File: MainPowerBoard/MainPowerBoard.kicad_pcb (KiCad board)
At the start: 2 copper layers, 177.8 x 177.8 mm, 259 parts, among them J101 CONN_01X04, J102 CONN_01X04, J103 CONN_01X04, J104 CONN_01X02, J105 CONN_01X02, J106 CONN_01X06, J107 CONN_01X06, J108 CONN_01X04, J109 CONN_01X04, J110 CONN_01X02, J111 CONN_01X02, J112 CONN_01X02, J113 CONN_01X02, J114 CONN_01X02, J115 CONN_01X02, J116 CONN_01X02, J117 CONN_01X02, J118 CONN_01X02, J119 CONN_01X02, J120 CONN_01X02, J121 CONN_01X02, J122 CONN_01X02, J123 CONN_01X02, J124 CONN_01X02, J125 CONN_01X02, J126 CONN_01X02, J127 CONN_01X02, J128 CONN_01X02, J129 CONN_01X02, J130 MOUNTING_HOLE, J131 MOUNTING_HOLE, J132 MOUNTING_HOLE, J133 MOUNTING_HOLE, Q1 CSD19502Q5B, Q2 CSD19502Q5B, SW701 KS-01Q-01, U1 LTC4357MPMS8, U1001 LMR16030S, U1101 LMR16030S, U1201 LMR16030S, U1301 LMR16030S, U1401 LMR16030S, U2 LTC4357MPMS8, U201 LMR16030S, U301 LMR16030S, U701 AP2204RA-5.0TRG1, U702 TLV271IDBVR, U703 LTC2950-1, U704 TLC393, U801 LMR16030S, U901 LMR16030S

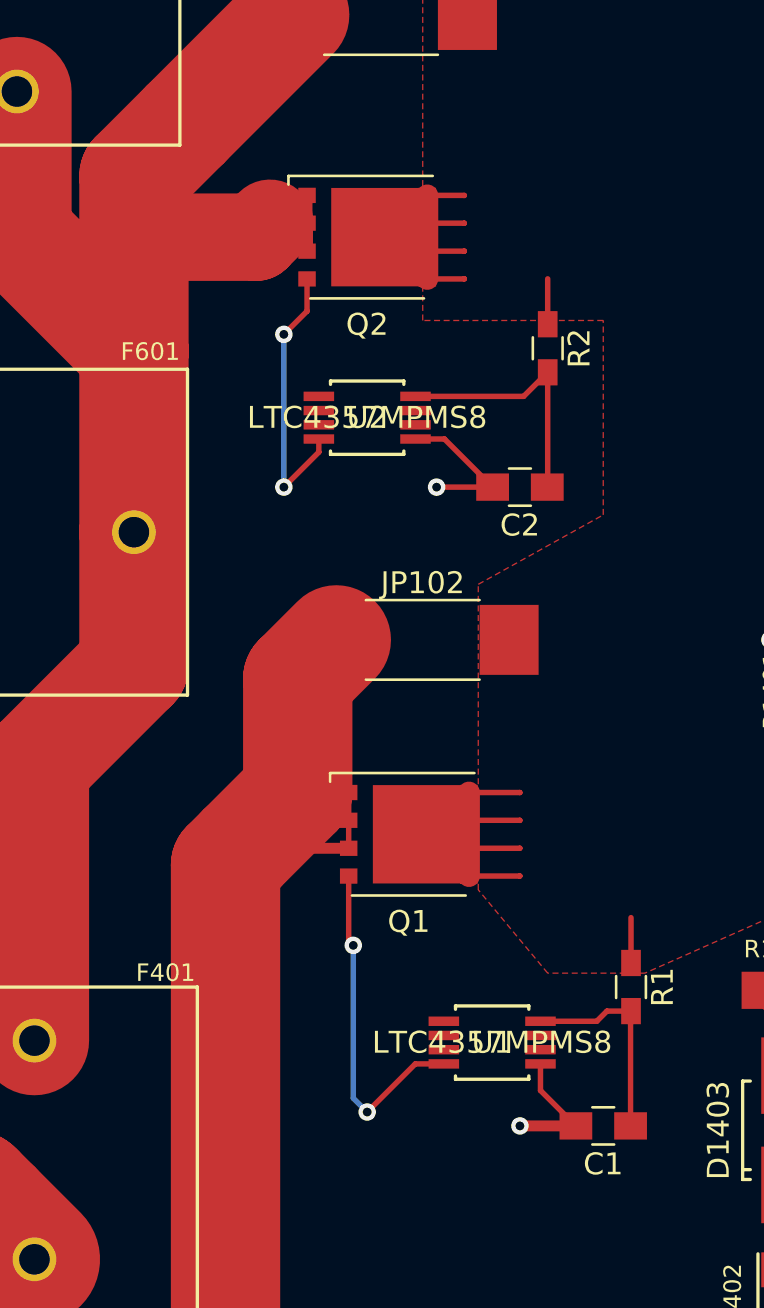
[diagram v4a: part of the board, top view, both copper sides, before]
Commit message: Fixed grounding of bat output and connected missing ground connection on LTC chip
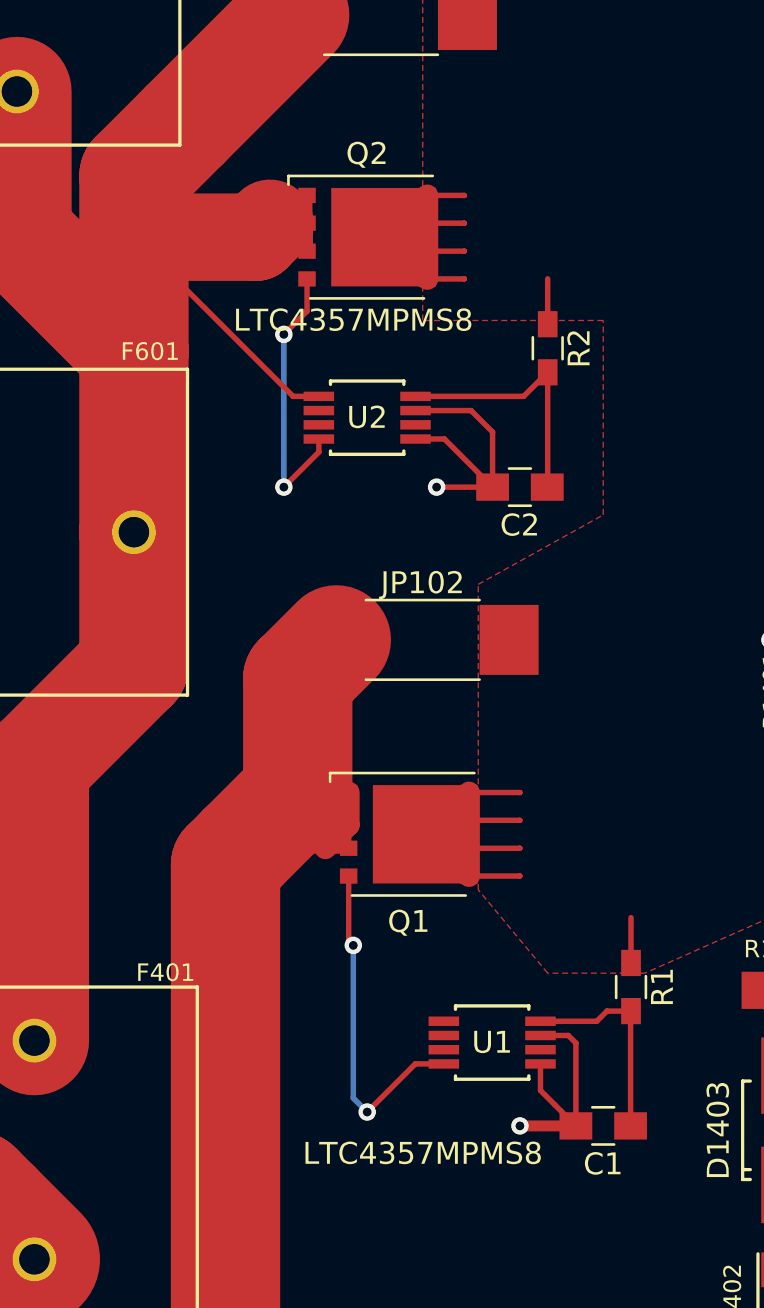
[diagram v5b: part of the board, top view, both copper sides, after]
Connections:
- F401 pad 2: GND -> /VCC_BATT_COMB
- F501 pad 2: GND -> /VCC_BATT_COMB
- F601 pad 2: GND -> /VCC_BATT_COMB
- JP103 pad 1: GND -> /VCC_BATT_COMB
- Q2 pad 1: GND -> /VCC_BATT_COMB
- Q2 pad 2: GND -> /VCC_BATT_COMB
- Q2 pad 3: GND -> /VCC_BATT_COMB
- U2 pad 1: GND -> /VCC_BATT_COMB
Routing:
- net /VCC_BATT_COMB: track 0.00 -> 87.7 mm
- net GND: track 698.8 -> 634.6 mm
- net /48V0_FROM_LINE: track 44.9 -> 47.9 mm
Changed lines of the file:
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@@
 (kicad_pcb (version 4) (host pcbnew 4.0.6)
   (general
-    (links 982)
-    (no_connects 356)
+    (links 981)
+    (no_connects 353)
     (area -6.075 -6.075 183.285 183.285)
     (thickness 1.6)
     (drawings 83)
-    (tracks 2097)
+    (tracks 2109)
     (zones 0)
     (modules 259)
-    (nets 151)
+    (nets 152)
   )
   (page B)
@@
   )
   (setup
-    (last_trace_width 0.5)
+    (last_trace_width 1)
     (user_trace_width 0.5)
     (user_trace_width 1)
@@
   (net 149 "/5 Volt Regulator -- 2/24V0_REG")
   (net 150 "Net-(D1402-Pad1)")
+  (net 151 /VCC_BATT_COMB)
   (net_class Default "This is the default net class."
     (clearance 0.2)
@@
     (add_net /STATE)
     (add_net /SW_HI)
+    (add_net /VCC_BATT_COMB)
     (add_net GND)
     (add_net "Net-(C1-Pad1)")
@@
       (net 77 "Net-(D401-Pad2)"))
     (pad 2 thru_hole circle (at 12.45 -7.45 90) (size 2 2) (drill 1.4) (layers *.Cu *.Mask)
-      (net 1 GND))
+      (net 151 /VCC_BATT_COMB))
   )
   (module CONN_PHOENIX_1844252_6PIN (layer F.Cu)
@@
       (net 81 "Net-(D601-Pad2)"))
     (pad 2 thru_hole circle (at 12.45 -7.45) (size 2 2) (drill 1.4) (layers *.Cu *.Mask)
-      (net 1 GND))
+      (net 151 /VCC_BATT_COMB))
   )
   (module Diodes_SMD:SMB_Handsoldering (layer F.Cu)
@@
       (net 79 "Net-(D501-Pad2)"))
     (pad 2 thru_hole circle (at 12.45 -7.45 270) (size 2 2) (drill 1.4) (layers *.Cu *.Mask)
-      (net 1 GND))
+      (net 151 /VCC_BATT_COMB))
   )
   (module hyperCustom:TP_SMT_Keystone (layer F.Cu)
@@
     (fp_line (start 5.55 1.85) (end -5.56 1.85) (layer F.CrtYd) (width 0.05))
     (pad 1 smd rect (at -3.95 0) (size 2.7 3.2) (layers F.Cu F.Paste F.Mask)
-      (net 1 GND))
+      (net 151 /VCC_BATT_COMB))
     (pad 2 smd rect (at 3.95 0) (size 2.7 3.2) (layers F.Cu F.Paste F.Mask)
       (net 126 /MAIN_POWER))
@@
     (tags "tdson ")
     (attr smd)
-    (fp_text reference Q2 (at 0 4) (layer F.SilkS)
+    (fp_text reference Q2 (at 0 -3.81) (layer F.SilkS)
       (effects (font (size 1 1) (thickness 0.15)))
     )
@@
     (fp_line (start -2 -2.6) (end -3 -1.6) (layer F.Fab) (width 0.1))
     (pad 1 smd rect (at -2.75 -1.91 270) (size 0.7 0.8) (layers F.Cu F.Paste F.Mask)
-      (net 1 GND))
+      (net 151 /VCC_BATT_COMB))
     (pad 2 smd rect (at -2.75 -0.64 270) (size 0.7 0.8) (layers F.Cu F.Paste F.Mask)
-      (net 1 GND))
+      (net 151 /VCC_BATT_COMB))
     (pad 3 smd rect (at -2.75 0.64 270) (size 0.7 0.8) (layers F.Cu F.Paste F.Mask)
-      (net 1 GND))
+      (net 151 /VCC_BATT_COMB))
     (pad 4 smd rect (at -2.75 1.91 270) (size 0.7 0.8) (layers F.Cu F.Paste F.Mask)
       (net 130 "Net-(Q2-Pad4)"))
@@
       (effects (font (size 1 1) (thickness 0.15)))
     )
-    (fp_text value LTC4357MPMS8 (at 0 0) (layer F.SilkS)
+    (fp_text value LTC4357MPMS8 (at -3.175 5.08) (layer F.SilkS)
       (effects (font (size 1 1) (thickness 0.15)))
     )
@@
     (fp_arc (start 0 -1.5494) (end 0.3048 -1.5494) (angle 180) (layer Dwgs.User) (width 0.1524))
     (pad 1 smd rect (at -2.2098 -0.974999) (size 1.397 0.4318) (layers F.Cu)
-      (net 28 /48V0_FROM_LINE))
+      (net 28 /48V0_FROM_LINE) (clearance 0.1))
     (pad 2 smd rect (at -2.2098 -0.325001) (size 1.397 0.4318) (layers F.Cu)
-      (net 131 "Net-(U1-Pad2)"))
+      (net 131 "Net-(U1-Pad2)") (clearance 0.1))
     (pad 3 smd rect (at -2.2098 0.325001) (size 1.397 0.4318) (layers F.Cu)
-      (net 132 "Net-(U1-Pad3)"))
+      (net 132 "Net-(U1-Pad3)") (clearance 0.1))
     (pad 4 smd rect (at -2.2098 0.974999) (size 1.397 0.4318) (layers F.Cu)
-      (net 129 "Net-(Q1-Pad4)"))
+      (net 129 "Net-(Q1-Pad4)") (clearance 0.1))
     (pad 5 smd rect (at 2.2098 0.974999) (size 1.397 0.4318) (layers F.Cu)
       (net 1 GND))
@@
       (effects (font (size 1 1) (thickness 0.15)))
     )
-    (fp_text value LTC4357MPMS8 (at 0 0) (layer F.SilkS)
+    (fp_text value LTC4357MPMS8 (at -0.635 -4.445) (layer F.SilkS)
       (effects (font (size 1 1) (thickness 0.15)))
     )
@@
     (fp_arc (start 0 -1.5494) (end 0.3048 -1.5494) (angle 180) (layer Dwgs.User) (width 0.1524))
     (pad 1 smd rect (at -2.2098 -0.974999) (size 1.397 0.4318) (layers F.Cu)
-      (net 1 GND) (clearance 0.1))
+      (net 151 /VCC_BATT_COMB) (clearance 0.1))
     (pad 2 smd rect (at -2.2098 -0.325001) (size 1.397 0.4318) (layers F.Cu)
       (net 134 "Net-(U2-Pad2)") (clearance 0.1))
@@
   (gr_line (start 177.8 0) (end 177.8 177.8) (angle 90) (layer Edge.Cuts) (width 0.15))
   (gr_line (start 0 0) (end 177.8 0) (angle 90) (layer Edge.Cuts) (width 0.15))
-  (segment (start 53.765 87) (end 53.765 84.45) (width 0.5) (layer F.Cu) (net 1) (status C00000))
-  (segment (start 45.85 86.36) (end 51.435 86.36) (width 4) (layer F.Cu) (net 1))
-  (segment (start 51.435 86.36) (end 52.07 85.725) (width 4) (layer F.Cu) (net 1))
+  (segment (start 64.4398 122.864999) (end 65.714999 122.864999) (width 0.25) (layer F.Cu) (net 1))
+  (segment (start 66.06 123.21) (end 66.06 127) (width 0.25) (layer F.Cu) (net 1))
+  (segment (start 65.714999 122.864999) (end 66.06 123.21) (width 0.25) (layer F.Cu) (net 1))
+  (segment (start 58.7248 94.289999) (end 61.269999 94.289999) (width 0.25) (layer F.Cu) (net 1))
+  (segment (start 62.25 95.27) (end 62.25 97.79) (width 0.25) (layer F.Cu) (net 1))
+  (segment (start 61.269999 94.289999) (end 62.25 95.27) (width 0.25) (layer F.Cu) (net 1))
   (segment (start 62.25 97.79) (end 59.69 97.79) (width 0.25) (layer F.Cu) (net 1))
   (via (at 59.69 97.79) (size 0.8) (drill 0.4) (layers F.Cu B.Cu) (net 1))
@@
   (via (at 63.5 127) (size 0.8) (drill 0.4) (layers F.Cu B.Cu) (net 1))
   (segment (start 64.4398 124.164999) (end 64.4398 125.3798) (width 0.25) (layer F.Cu) (net 1))
-  (segment (start 64.4398 125.3798) (end 66.06 127) (width 0.25) (layer F.Cu) (net 1))
+  (segment (start 64.4398 125.3798) (end 65.0975 126.0375) (width 0.25) (layer F.Cu) (net 1))
+  (segment (start 65.0975 126.0375) (end 66.06 127) (width 0.25) (layer F.Cu) (net 1))
   (via (at 93.38 67.945) (size 1) (drill 0.3) (layers F.Cu B.Cu) (net 1))
   (via (at 95.38 65.245) (size 1) (drill 0.3) (layers F.Cu B.Cu) (net 1))
@@
   (via (at 88.235 117.2) (size 1) (drill 0.3) (layers F.Cu B.Cu) (net 1))
   (via (at 89.835 114.7) (size 1) (drill 0.3) (layers F.Cu B.Cu) (net 1))
-  (segment (start 53.765 87) (end 53.765 85.72) (width 0.5) (layer F.Cu) (net 1))
-  (segment (start 45.85 91.57) (end 45.85 86.36) (width 5) (layer F.Cu) (net 1))
-  (segment (start 48.19 81.21) (end 53.2 76.2) (width 5) (layer F.Cu) (net 1))
-  (segment (start 45.85 83.55) (end 48.19 81.21) (width 5) (layer F.Cu) (net 1))
-  (segment (start 45.85 86.36) (end 45.85 83.55) (width 5) (layer F.Cu) (net 1))
-  (segment (start 40.5 79.7) (end 40.5 86.22) (width 5) (layer F.Cu) (net 1))
-  (segment (start 45.85 91.57) (end 45.85 99.85) (width 5) (layer F.Cu) (net 1))
-  (segment (start 40.5 86.22) (end 45.85 91.57) (width 5) (layer F.Cu) (net 1))
-  (segment (start 41.3 123.1) (end 41.3 110.515) (width 5) (layer F.Cu) (net 1))
-  (segment (start 45.85 105.965) (end 45.85 99.85) (width 5) (layer F.Cu) (net 1))
-  (segment (start 41.3 110.515) (end 45.85 105.965) (width 5) (layer F.Cu) (net 1))
   (via (at 83.335 125.4) (size 0.8) (drill 0.4) (layers F.Cu B.Cu) (net 1))
   (segment (start 82.985 125.75) (end 83.335 125.4) (width 0.25) (layer F.Cu) (net 1))
@@
   (segment (start 130.48014 168.2) (end 126.59936 168.2) (width 0.25) (layer F.Cu) (net 26))
   (segment (start 75.435 139.6) (end 75.435 136.41986) (width 0.25) (layer F.Cu) (net 27))
-  (segment (start 55.67 114.305) (end 50.795 114.305) (width 0.5) (layer F.Cu) (net 28))
+  (segment (start 55.67 111.755) (end 55.67 113.24) (width 1) (layer F.Cu) (net 28) (status C00000))
+  (segment (start 55.67 113.24) (end 54.605 114.305) (width 1) (layer F.Cu) (net 28) (status 400000))
+  (segment (start 55.67 114.305) (end 54.605 114.305) (width 0.5) (layer F.Cu) (net 28))
+  (segment (start 54.605 114.305) (end 50.795 114.305) (width 0.5) (layer F.Cu) (net 28))
   (segment (start 50.795 114.305) (end 50.8 114.3) (width 0.5) (layer F.Cu) (net 28))
   (segment (start 55.67 111.755) (end 55.67 113.025) (width 0.25) (layer F.Cu) (net 28))
@@
   (segment (start 79.685 136.55) (end 84.035 140.9) (width 3) (layer F.Cu) (net 149))
   (segment (start 75.435 133.58014) (end 75.435 129.69936) (width 0.25) (layer F.Cu) (net 150))
+  (segment (start 54.3052 93.640001) (end 53.130001 93.640001) (width 0.25) (layer F.Cu) (net 151))
+  (segment (start 53.130001 93.640001) (end 45.85 86.36) (width 0.25) (layer F.Cu) (net 151))
+  (segment (start 53.765 87) (end 53.765 84.45) (width 0.5) (layer F.Cu) (net 151))
+  (segment (start 45.85 86.36) (end 51.435 86.36) (width 4) (layer F.Cu) (net 151))
+  (segment (start 51.435 86.36) (end 52.07 85.725) (width 4) (layer F.Cu) (net 151))
+  (segment (start 53.765 87) (end 53.765 85.72) (width 0.5) (layer F.Cu) (net 151))
+  (segment (start 45.85 91.57) (end 45.85 86.36) (width 5) (layer F.Cu) (net 151))
+  (segment (start 48.19 81.21) (end 53.2 76.2) (width 5) (layer F.Cu) (net 151))
+  (segment (start 45.85 83.55) (end 48.19 81.21) (width 5) (layer F.Cu) (net 151))
+  (segment (start 45.85 86.36) (end 45.85 83.55) (width 5) (layer F.Cu) (net 151))
+  (segment (start 40.5 79.7) (end 40.5 86.22) (width 5) (layer F.Cu) (net 151))
+  (segment (start 45.85 91.57) (end 45.85 99.85) (width 5) (layer F.Cu) (net 151))
+  (segment (start 40.5 86.22) (end 45.85 91.57) (width 5) (layer F.Cu) (net 151))
+  (segment (start 41.3 123.1) (end 41.3 110.515) (width 5) (layer F.Cu) (net 151))
+  (segment (start 45.85 105.965) (end 45.85 99.85) (width 5) (layer F.Cu) (net 151))
+  (segment (start 41.3 110.515) (end 45.85 105.965) (width 5) (layer F.Cu) (net 151))
   (zone (net 49) (net_name /GND_FROM_LINE) (layer B.Cu) (hatch edge 0.508)
     (priority 1)
